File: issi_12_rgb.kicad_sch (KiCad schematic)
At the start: 26 parts, among them Q1 3412, Q10 3412, Q11 3412, Q12 3412, Q13 3412, Q14 3412, Q15 3412, Q16 3412, Q2 3412, Q3 3412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

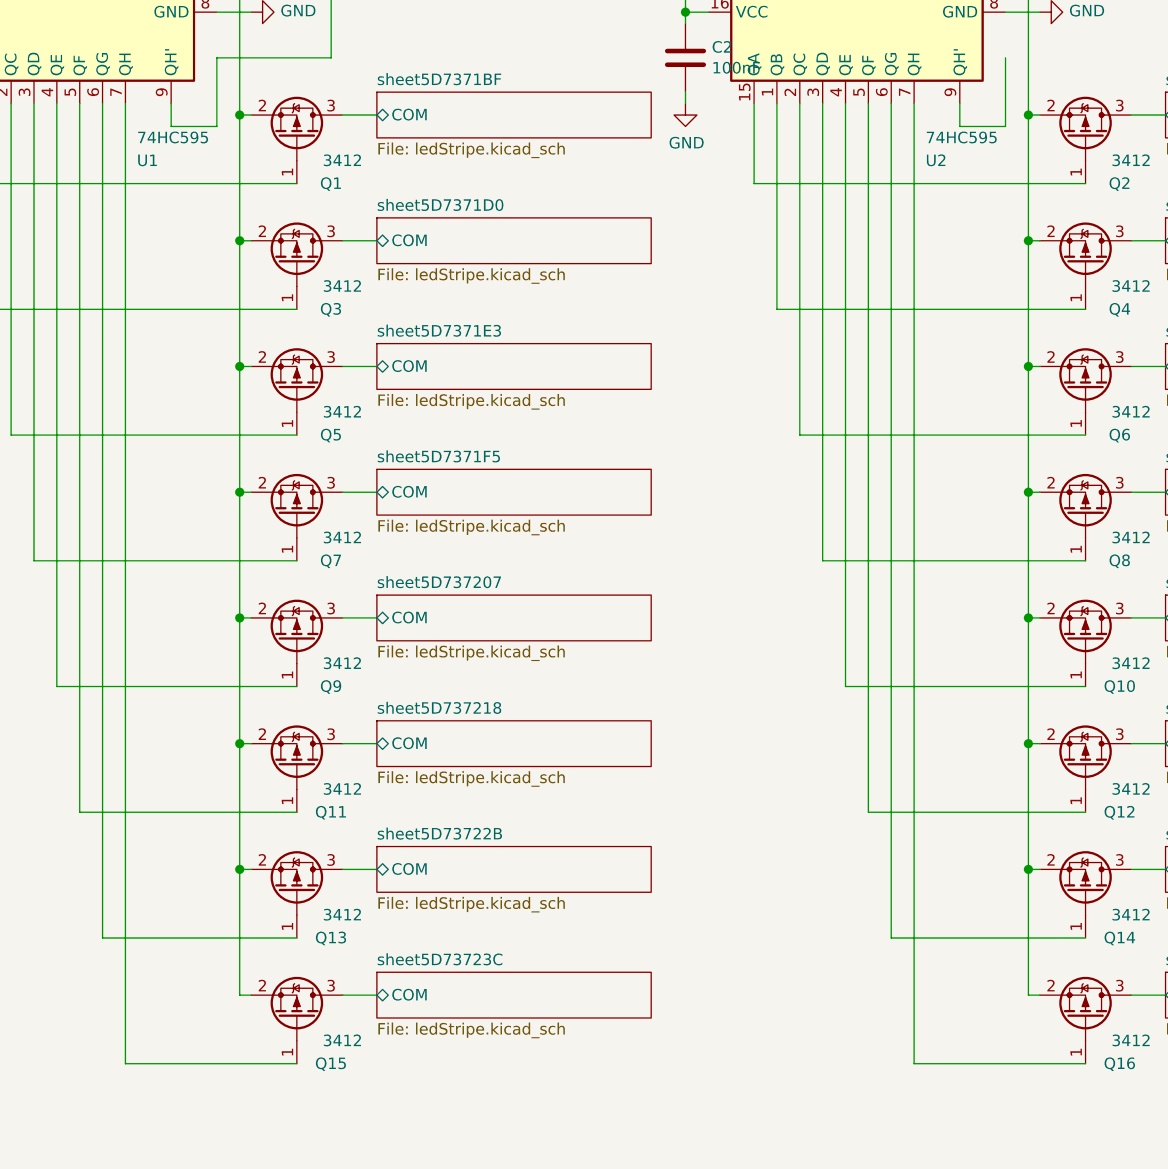
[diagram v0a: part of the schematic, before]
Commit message: Changed FETs to SOT-23 and buttons to something that is more boring
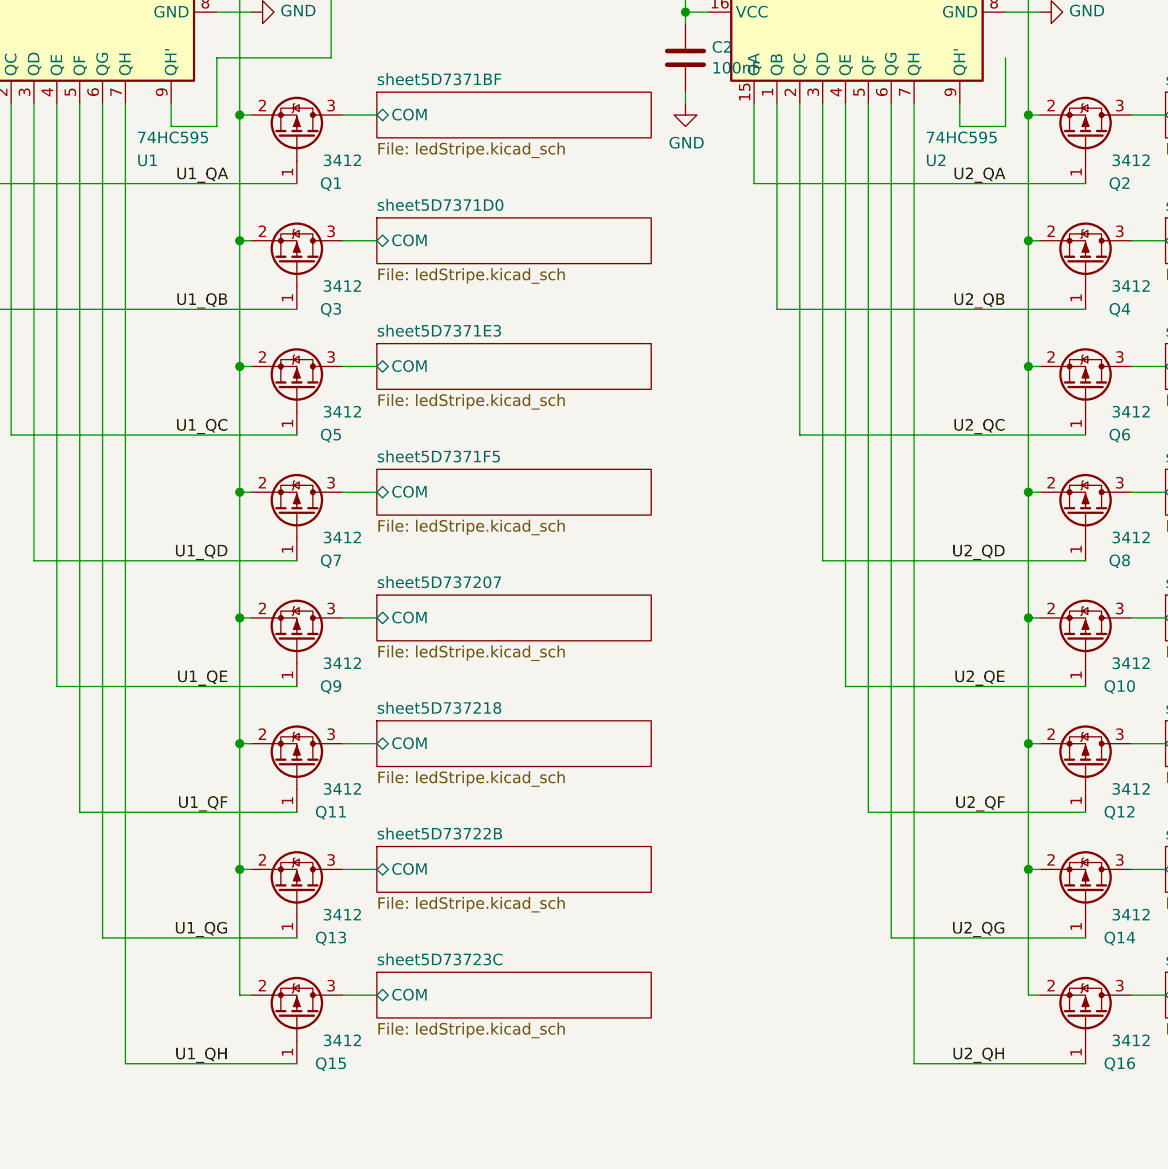
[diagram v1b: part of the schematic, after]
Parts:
- C1, C2, C3, C4: LCSC (none) -> C14663
- Q1, Q10, Q11, Q12, Q13, Q14, Q15, Q16, Q2, Q3, Q4, Q5, Q6, Q7, Q8, Q9: footprint Package_TO_SOT_SMD:SOT-883 -> Package_TO_SOT_SMD:SOT-23; LCSC (none) -> C15127
- R1, R2: LCSC (none) -> C23186
- U1, U2: LCSC (none) -> C5948
- U3, U4: LCSC (none) -> DNP
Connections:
- net U2_QC: now reaches Q6.1 (G), U2.2 (QC)
- net U2_QD: now reaches Q8.1 (G), U2.3 (QD)
- net U1_QC: now reaches Q5.1 (G), U1.2 (QC)
- net U2_QB: now reaches Q4.1 (G), U2.1 (QB)
- net U2_QA: now reaches Q2.1 (G), U2.15 (QA)
- net U2_QE: now reaches Q10.1 (G), U2.4 (QE)
- net U2_QF: now reaches Q12.1 (G), U2.5 (QF)
- net U2_QG: now reaches Q14.1 (G), U2.6 (QG)
- net U2_QH: now reaches Q16.1 (G), U2.7 (QH)
- net U1_QB: now reaches Q3.1 (G), U1.1 (QB)
- net U1_QA: now reaches Q1.1 (G), U1.15 (QA)
- net U1_QD: now reaches Q7.1 (G), U1.3 (QD)
- net U1_QE: now reaches Q9.1 (G), U1.4 (QE)
- net U1_QF: now reaches Q11.1 (G), U1.5 (QF)
- net U1_QG: now reaches Q13.1 (G), U1.6 (QG)
- net U1_QH: now reaches Q15.1 (G), U1.7 (QH)
